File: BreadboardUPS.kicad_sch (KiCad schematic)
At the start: 3 parts, among them J2 Conn_01x04_Pin, J3 Conn_01x02_Pin, J4 Conn_01x02_Pin

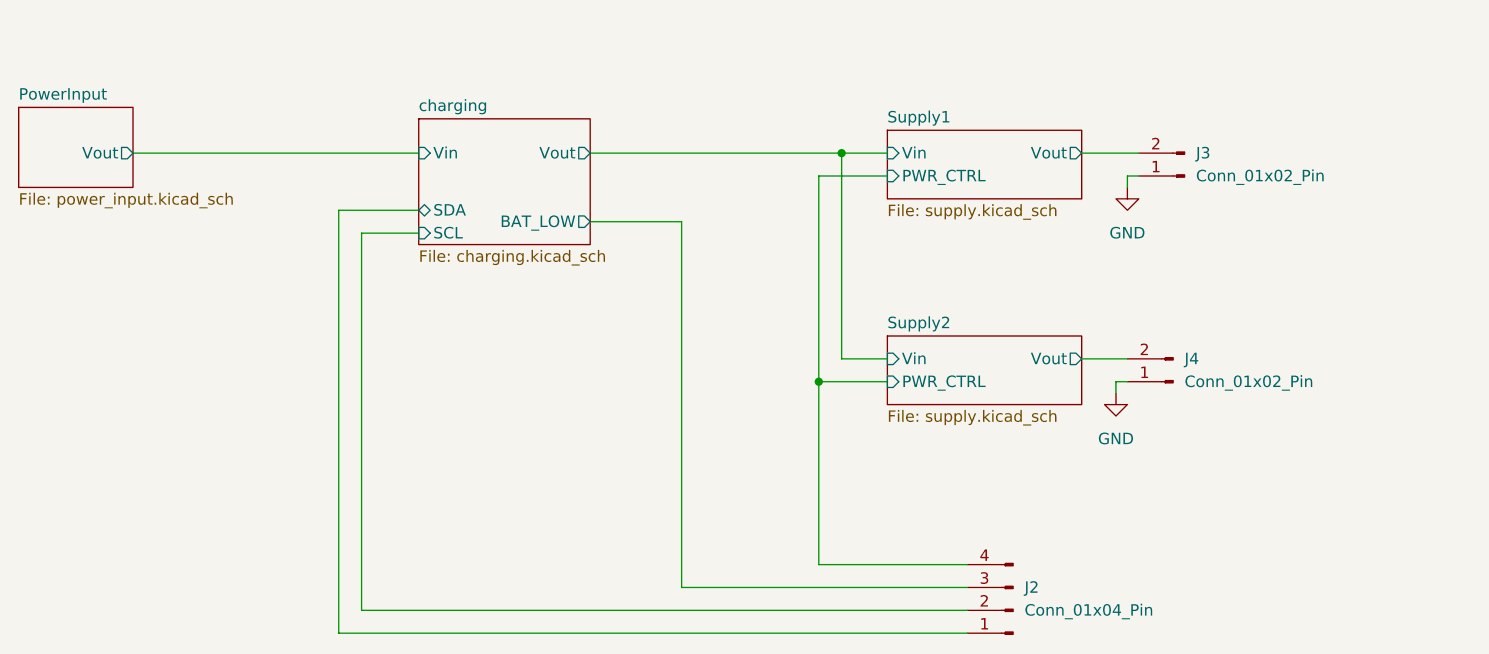
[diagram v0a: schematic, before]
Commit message: Solder jumpers for smaller simpler supply
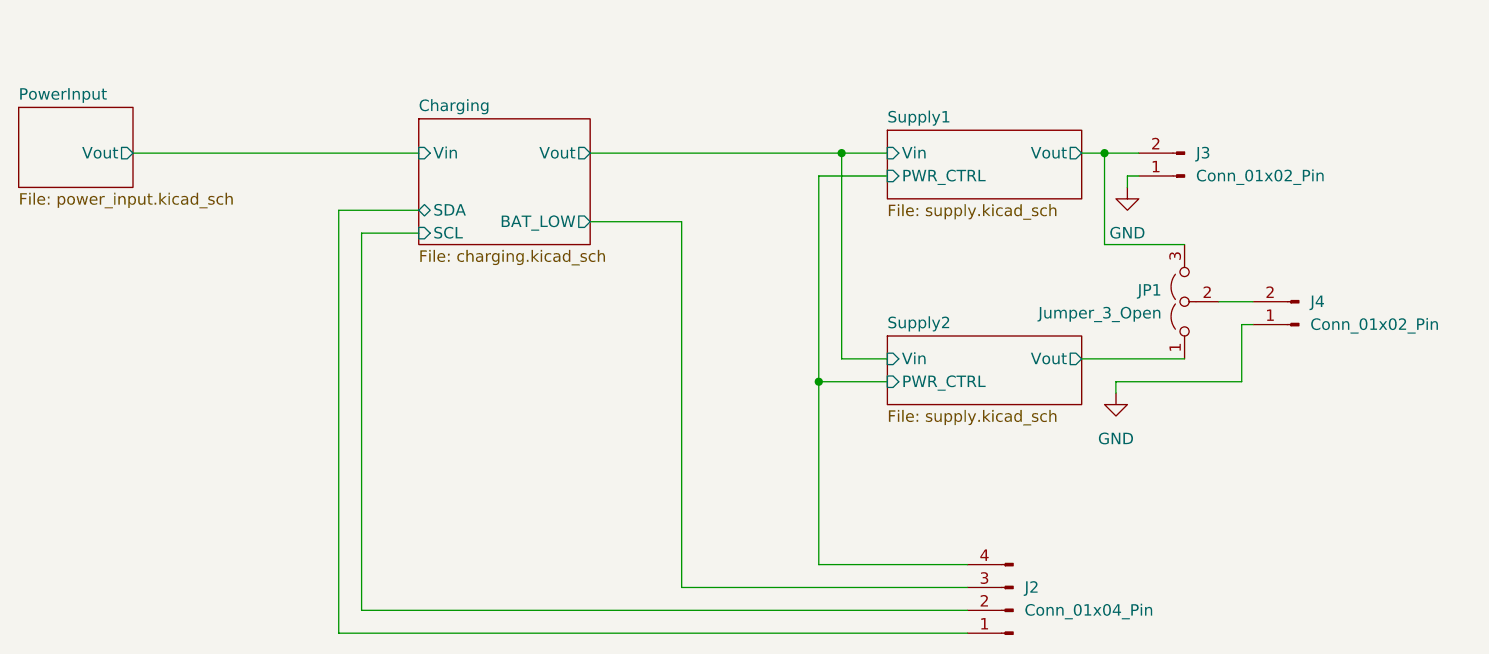
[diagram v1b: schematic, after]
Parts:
- added JP1: Jumper_3_Open, symbol Jumper:Jumper_3_Open
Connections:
- net Supply1/Vout: now also JP1.3 (B)
- net Supply2/Vout: now also JP1.1 (A); no longer J4.2 (Pin_2)
- new net: J4.2 (Pin_2), JP1.2 (C)
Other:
- sheet charging renamed Charging
- moved on the sheet: J4
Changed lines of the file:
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@@
+	)
+	(junction
+		(at 203.2 76.2)
+		(diameter 0)
+		(color 0 0 0 0)
 	)
 	(junction
@@
 	(wire
 		(pts
+			(xy 218.44 101.6) (xy 218.44 95.25)
+		)
+		(stroke
+			(width 0)
+			(type default)
+		)
+	)
+	(wire
+		(pts
 			(xy 171.45 101.6) (xy 171.45 121.92)
 		)
@@
 	(wire
 		(pts
-			(xy 204.47 101.6) (xy 205.74 101.6)
+			(xy 215.9 92.71) (xy 219.71 92.71)
 		)
 		(stroke
@@
 	(wire
 		(pts
+			(xy 200.66 99.06) (xy 212.09 99.06)
+		)
+		(stroke
+			(width 0)
+			(type default)
+		)
+	)
+	(wire
+		(pts
 			(xy 118.11 129.54) (xy 187.96 129.54)
 		)
@@
 	(wire
 		(pts
+			(xy 218.44 95.25) (xy 219.71 95.25)
+		)
+		(stroke
+			(width 0)
+			(type default)
+		)
+	)
+	(wire
+		(pts
+			(xy 203.2 76.2) (xy 207.01 76.2)
+		)
+		(stroke
+			(width 0)
+			(type default)
+		)
+	)
+	(wire
+		(pts
+			(xy 204.47 101.6) (xy 218.44 101.6)
+		)
+		(stroke
+			(width 0)
+			(type default)
+		)
+	)
+	(wire
+		(pts
 			(xy 120.65 127) (xy 187.96 127)
 		)
@@
 	(wire
 		(pts
+			(xy 203.2 86.36) (xy 203.2 76.2)
+		)
+		(stroke
+			(width 0)
+			(type default)
+		)
+	)
+	(wire
+		(pts
+			(xy 212.09 86.36) (xy 203.2 86.36)
+		)
+		(stroke
+			(width 0)
+			(type default)
+		)
+	)
+	(wire
+		(pts
 			(xy 171.45 121.92) (xy 187.96 121.92)
 		)
@@
 	(wire
 		(pts
-			(xy 200.66 76.2) (xy 207.01 76.2)
+			(xy 200.66 76.2) (xy 203.2 76.2)
 		)
 		(stroke
@@
 		(pts
 			(xy 205.74 78.74) (xy 205.74 80.01)
-		)
-		(stroke
-			(width 0)
-			(type default)
-		)
-	)
-	(wire
-		(pts
-			(xy 200.66 99.06) (xy 205.74 99.06)
 		)
 		(stroke
@@
 	(symbol
 		(lib_id "Connector:Conn_01x02_Pin")
-		(at 210.82 101.6 180)
+		(at 224.79 95.25 180)
 		(unit 1)
 		(exclude_from_sim no)
@@
 		(fields_autoplaced yes)
 		(property "Reference" "J4"
-			(at 212.09 99.0599 0)
+			(at 226.06 92.7099 0)
 			(effects
 				(font
@@
 		)
 		(property "Value" "Conn_01x02_Pin"
-			(at 212.09 101.5999 0)
+			(at 226.06 95.2499 0)
 			(effects
 				(font
@@
 		)
 		(property "Footprint" ""
-			(at 210.82 101.6 0)
+			(at 224.79 95.25 0)
 			(effects
 				(font
@@
 		)
 		(property "Datasheet" "~"
-			(at 210.82 101.6 0)
+			(at 224.79 95.25 0)
 			(effects
 				(font
@@
 		)
 		(property "Description" "Generic connector, single row, 01x02, script generated"
-			(at 210.82 101.6 0)
+			(at 224.79 95.25 0)
 			(effects
 				(font
@@
 		)
 	)
+	(symbol
+		(lib_id "Jumper:Jumper_3_Open")
+		(at 212.09 92.71 90)
+		(unit 1)
+		(exclude_from_sim no)
+		(in_bom no)
+		(on_board yes)
+		(dnp no)
+		(fields_autoplaced yes)
+		(property "Reference" "JP1"
+			(at 209.55 91.4399 90)
+			(effects
+				(font
+					(size 1.27 1.27)
+				)
+				(justify left)
+			)
+		)
+		(property "Value" "Jumper_3_Open"
+			(at 209.55 93.9799 90)
+			(effects
+				(font
+					(size 1.27 1.27)
+				)
+				(justify left)
+			)
+		)
+		(property "Footprint" ""
+			(at 212.09 92.71 0)
+			(effects
+				(font
+					(size 1.27 1.27)
+				)
+				(hide yes)
+			)
+		)
+		(property "Datasheet" "~"
+			(at 212.09 92.71 0)
+			(effects
+				(font
+					(size 1.27 1.27)
+				)
+				(hide yes)
+			)
+		)
+		(property "Description" "Jumper, 3-pole, both open"
+			(at 212.09 92.71 0)
+			(effects
+				(font
+					(size 1.27 1.27)
+				)
+				(hide yes)
+			)
+		)
+		(pin "3"
+		)
+		(pin "2"
+		)
+		(pin "1"
+		)
+		(instances
+			(project ""
+				(path "/3f1ccd97-6ac6-4e7a-a00a-840cd07719d8"
+					(reference "JP1")
+					(unit 1)
+				)
+			)
+		)
+	)
 	(sheet
 		(at 179.07 73.66)
@@
 			(color 0 0 0 0.0000)
 		)
-		(property "Sheetname" "charging"
+		(property "Sheetname" "Charging"
 			(at 127 71.6784 0)
 			(effects

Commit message: Part selection
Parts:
- removed JP1: Jumper_3_Open, symbol Jumper:Jumper_3_Open
- added JP101: SolderJumper_3_Open, Jumper:SolderJumper-3_P1.3mm_Open_RoundedPad1.0x1.5mm, symbol Jumper:SolderJumper_3_Open
- J101: renamed from J2; footprint (none) -> Connector_PinHeader_2.54mm:PinHeader_1x04_P2.54mm_Vertical; now left out of the parts list
- J102: renamed from J3; footprint (none) -> Connector_PinHeader_2.54mm:PinHeader_1x02_P2.54mm_Vertical; now left out of the parts list
- J103: renamed from J4; footprint (none) -> Connector_PinHeader_2.54mm:PinHeader_1x02_P2.54mm_Vertical; now left out of the parts list
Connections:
- net Supply1/Vout: now also JP101.3 (B)
- net Supply2/Vout: now also JP101.1 (A)
- net at J103.2 (Pin_2): now also JP101.2 (C)
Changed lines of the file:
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@@
+	(wire
+		(pts
+			(xy 212.09 86.36) (xy 212.09 87.63)
+		)
+		(stroke
+			(width 0)
+			(type default)
+		)
+	)
 	(wire
 		(pts
@@
 		(pts
 			(xy 173.99 76.2) (xy 179.07 76.2)
+		)
+		(stroke
+			(width 0)
+			(type default)
+		)
+	)
+	(wire
+		(pts
+			(xy 212.09 97.79) (xy 212.09 99.06)
 		)
 		(stroke
@@
 		(unit 1)
 		(exclude_from_sim no)
-		(in_bom yes)
+		(in_bom no)
 		(on_board yes)
 		(dnp no)
 		(fields_autoplaced yes)
-		(property "Reference" "J4"
+		(property "Reference" "J103"
 			(at 226.06 92.7099 0)
 			(effects
@@
 			)
 		)
-		(property "Footprint" ""
+		(property "Footprint" "Connector_PinHeader_2.54mm:PinHeader_1x02_P2.54mm_Vertical"
 			(at 224.79 95.25 0)
 			(effects
@@
 			(project "BreadboardUPS"
 				(path "/3f1ccd97-6ac6-4e7a-a00a-840cd07719d8"
-					(reference "J4")
+					(reference "J103")
 					(unit 1)
 				)
@@
 		(unit 1)
 		(exclude_from_sim no)
-		(in_bom yes)
+		(in_bom no)
 		(on_board yes)
 		(dnp no)
 		(fields_autoplaced yes)
-		(property "Reference" "J2"
+		(property "Reference" "J101"
 			(at 194.31 124.4599 0)
 			(effects
@@
 			)
 		)
-		(property "Footprint" ""
+		(property "Footprint" "Connector_PinHeader_2.54mm:PinHeader_1x04_P2.54mm_Vertical"
 			(at 193.04 127 0)
 			(effects
@@
 			(project ""
 				(path "/3f1ccd97-6ac6-4e7a-a00a-840cd07719d8"
-					(reference "J2")
+					(reference "J101")
 					(unit 1)
 				)
@@
 		(dnp no)
 		(fields_autoplaced yes)
-		(property "Reference" "#PWR015"
+		(property "Reference" "#PWR0101"
 			(at 204.47 109.22 0)
 			(effects
@@
 			(project "BreadboardUPS"
 				(path "/3f1ccd97-6ac6-4e7a-a00a-840cd07719d8"
-					(reference "#PWR015")
+					(reference "#PWR0101")
 					(unit 1)
 				)
@@
 		(unit 1)
 		(exclude_from_sim no)
-		(in_bom yes)
+		(in_bom no)
 		(on_board yes)
 		(dnp no)
 		(fields_autoplaced yes)
-		(property "Reference" "J3"
+		(property "Reference" "J102"
 			(at 213.36 76.1999 0)
 			(effects
@@
 			)
 		)
-		(property "Footprint" ""
+		(property "Footprint" "Connector_PinHeader_2.54mm:PinHeader_1x02_P2.54mm_Vertical"
 			(at 212.09 78.74 0)
 			(effects
@@
 			(project ""
 				(path "/3f1ccd97-6ac6-4e7a-a00a-840cd07719d8"
-					(reference "J3")
+					(reference "J102")
+					(unit 1)
+				)
+			)
+		)
+	)
+	(symbol
+		(lib_id "Jumper:SolderJumper_3_Open")
+		(at 212.09 92.71 90)
+		(unit 1)
+		(exclude_from_sim no)
+		(in_bom no)
+		(on_board yes)
+		(dnp no)
+		(fields_autoplaced yes)
+		(property "Reference" "JP101"
+			(at 209.55 91.4399 90)
+			(effects
+				(font
+					(size 1.27 1.27)
+				)
+				(justify left)
+			)
+		)
+		(property "Value" "SolderJumper_3_Open"
+			(at 209.55 93.9799 90)
+			(effects
+				(font
+					(size 1.27 1.27)
+				)
+				(justify left)
+			)
+		)
+		(property "Footprint" "Jumper:SolderJumper-3_P1.3mm_Open_RoundedPad1.0x1.5mm"
+			(at 212.09 92.71 0)
+			(effects
+				(font
+					(size 1.27 1.27)
+				)
+				(hide yes)
+			)
+		)
+		(property "Datasheet" "~"
+			(at 212.09 92.71 0)
+			(effects
+				(font
+					(size 1.27 1.27)
+				)
+				(hide yes)
+			)
+		)
+		(property "Description" "Solder Jumper, 3-pole, open"
+			(at 212.09 92.71 0)
+			(effects
+				(font
+					(size 1.27 1.27)
+				)
+				(hide yes)
+			)
+		)
+		(pin "2"
+		)
+		(pin "3"
+		)
+		(pin "1"
+		)
+		(instances
+			(project ""
+				(path "/3f1ccd97-6ac6-4e7a-a00a-840cd07719d8"
+					(reference "JP101")
 					(unit 1)
 				)
@@
 		(dnp no)
 		(fields_autoplaced yes)
-		(property "Reference" "#PWR014"
+		(property "Reference" "#PWR0102"
 			(at 205.74 86.36 0)
 			(effects
@@
 			(project "BreadboardUPS"
 				(path "/3f1ccd97-6ac6-4e7a-a00a-840cd07719d8"
-					(reference "#PWR014")
+					(reference "#PWR0102")
 					(unit 1)
 				)
-			)
-		)
-	)
-	(symbol
-		(lib_id "Jumper:Jumper_3_Open")
-		(at 212.09 92.71 90)
-		(unit 1)
-		(exclude_from_sim no)
-		(in_bom no)
-		(on_board yes)
-		(dnp no)
-		(fields_autoplaced yes)
-		(property "Reference" "JP1"
-			(at 209.55 91.4399 90)
-			(effects
-				(font
-					(size 1.27 1.27)
-				)
-				(justify left)
-			)
-		)
-		(property "Value" "Jumper_3_Open"
-			(at 209.55 93.9799 90)
-			(effects
-				(font
-					(size 1.27 1.27)
-				)
-				(justify left)
-			)
-		)
-		(property "Footprint" ""
-			(at 212.09 92.71 0)
-			(effects
-				(font
-					(size 1.27 1.27)
-				)
-				(hide yes)
-			)
-		)
-		(property "Datasheet" "~"
-			(at 212.09 92.71 0)
-			(effects
-				(font
-					(size 1.27 1.27)
-				)
-				(hide yes)
-			)
-		)
-		(property "Description" "Jumper, 3-pole, both open"
-			(at 212.09 92.71 0)
-			(effects
-				(font
-					(size 1.27 1.27)
-				)
-				(hide yes)
-			)
-		)
-		(pin "3"
-		)
-		(pin "2"
-		)
-		(pin "1"
-		)
-		(instances
-			(project ""
-				(path "/3f1ccd97-6ac6-4e7a-a00a-840cd07719d8"
-					(reference "JP1")
-					(unit 1)
-				)

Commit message: Connection naming
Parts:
- removed J101: Conn_01x04_Pin, Connector_PinHeader_2.54mm:PinHeader_1x04_P2.54mm_Vertical, symbol Connector:Conn_01x04_Pin
- added J101: Output1, Connector_PinHeader_2.54mm:PinHeader_1x02_P2.54mm_Vertical, symbol Connector:Conn_01x02_Pin
- added J104: Ctrl, Connector_PinHeader_2.54mm:PinHeader_1x05_P2.54mm_Vertical, symbol Connector:Conn_01x05_Pin
- added J105, J106, J107: Output2, Connector_PinHeader_2.54mm:PinHeader_1x02_P2.54mm_Vertical, symbol Connector:Conn_01x02_Pin
- J102, J103: value Conn_01x02_Pin -> Output1
- JP101: value SolderJumper_3_Open -> Single/Dual Supply
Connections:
- net GND: now also J102.2 (Pin_2), J103.2 (Pin_2), J101.2 (Pin_2), J105.2 (Pin_2), J106.2 (Pin_2), J107.2 (Pin_2); no longer J102.1 (Pin_1), J103.1 (Pin_1)
- net Supply1/Vout: now also J102.1 (Pin_1), J103.1 (Pin_1), J101.1 (Pin_1); no longer J102.2 (Pin_2)
- net at JP101.2 (C): now also J105.1 (Pin_1), J106.1 (Pin_1), J107.1 (Pin_1); no longer J103.2 (Pin_2)
- new net BAT_LOW: J104.3 (Pin_3)
- new net PFM: J104.1 (Pin_1)
- new net PWR_CTRL: J104.2 (Pin_2)
- new net SCL: J104.5 (Pin_5)
- new net SDA: J104.4 (Pin_4)
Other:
- sheet Supply1 ports: added PFM; removed none
- sheet Supply2 ports: added PFM; removed none

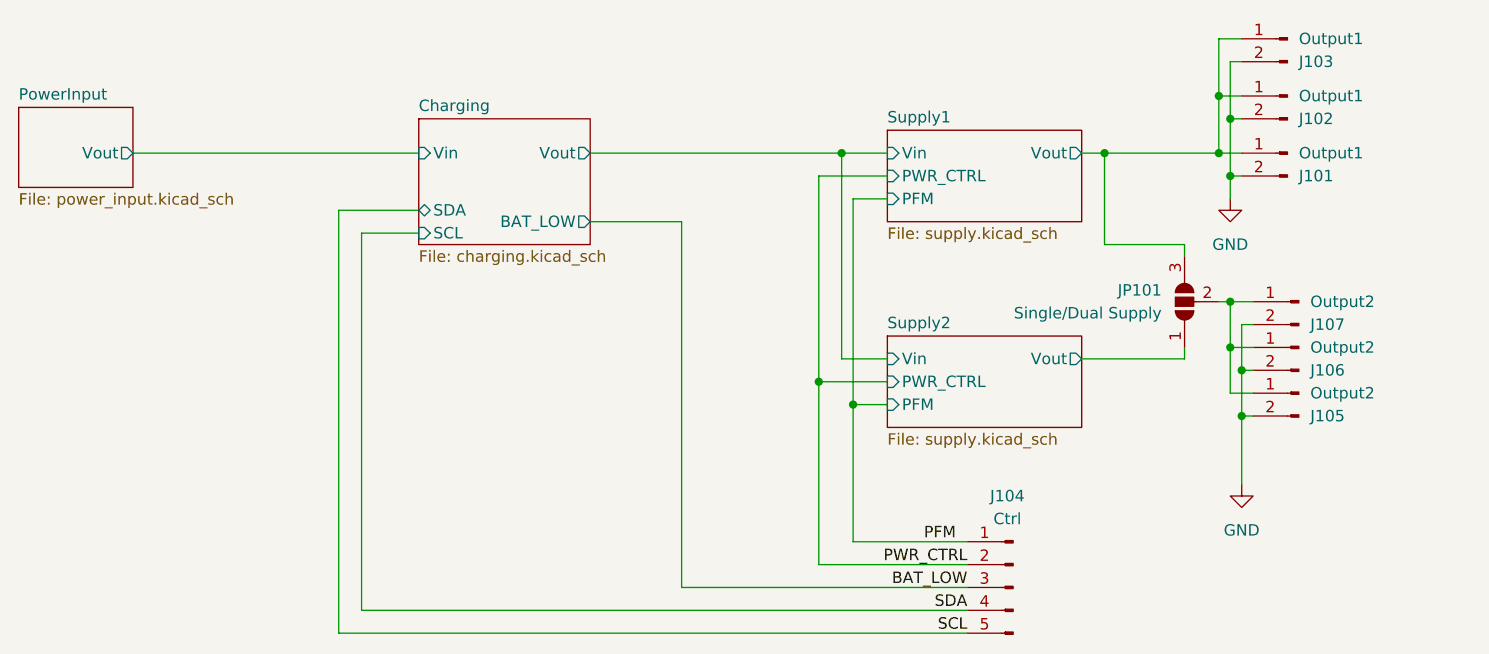
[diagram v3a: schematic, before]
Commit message: Remove dual supply
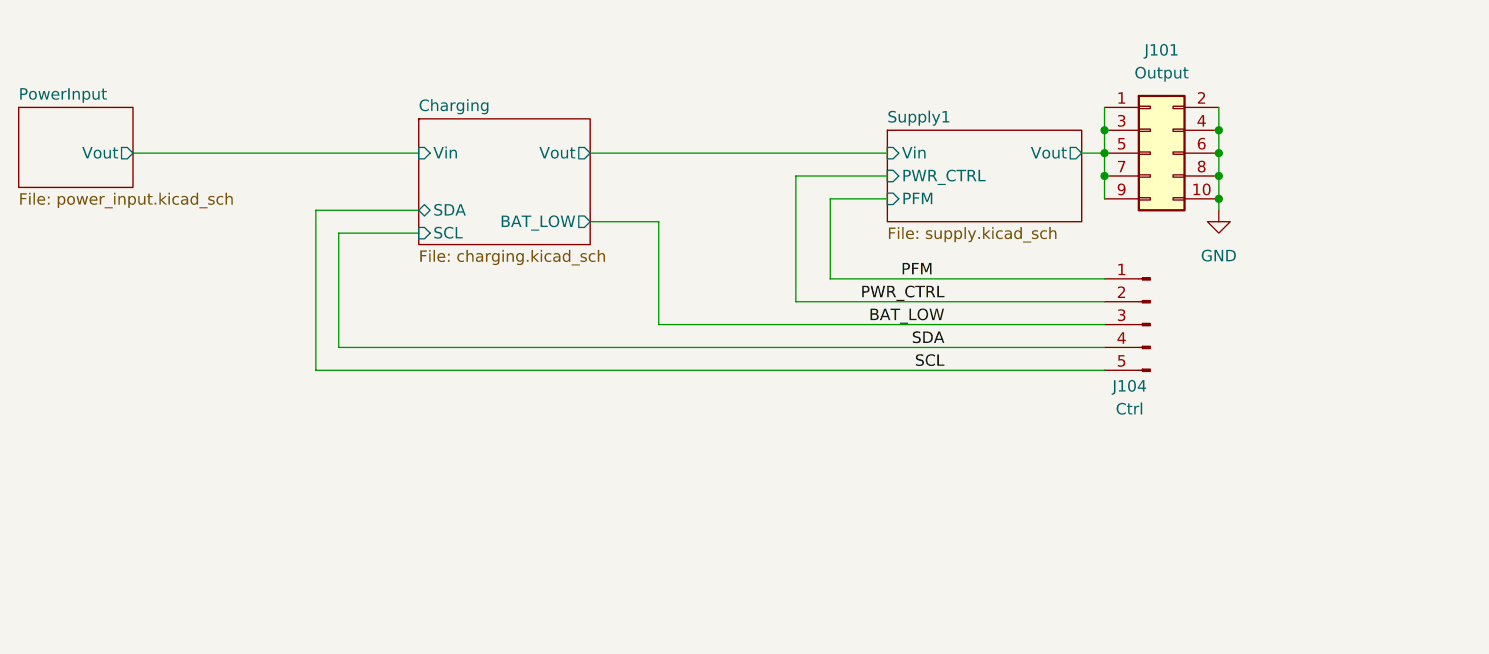
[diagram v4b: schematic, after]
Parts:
- removed J101, J102, J103: Output1, Connector_PinHeader_2.54mm:PinHeader_1x02_P2.54mm_Vertical, symbol Connector:Conn_01x02_Pin
- removed J105, J106, J107: Output2, Connector_PinHeader_2.54mm:PinHeader_1x02_P2.54mm_Vertical, symbol Connector:Conn_01x02_Pin
- removed JP101: Single/Dual Supply, Jumper:SolderJumper-3_P1.3mm_Open_RoundedPad1.0x1.5mm, symbol Jumper:SolderJumper_3_Open
- added J101: Output, Connector_PinHeader_2.54mm:PinHeader_2x05_P2.54mm_Vertical, symbol Connector_Generic:Conn_02x05_Odd_Even
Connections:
- net GND: now also J101.10 (Pin_10), J101.2 (Pin_2), J101.4 (Pin_4), J101.6 (Pin_6), J101.8 (Pin_8)
- net Supply1/Vout: now also J101.1 (Pin_1), J101.3 (Pin_3), J101.5 (Pin_5), J101.7 (Pin_7), J101.9 (Pin_9)
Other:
- removed sheet Supply2
- moved on the sheet: J104

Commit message: Update BOM options for export
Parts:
- J101, J104: now left out of the parts list
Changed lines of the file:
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@@
 		(unit 1)
 		(exclude_from_sim no)
-		(in_bom yes)
+		(in_bom no)
 		(on_board yes)
 		(dnp no)
@@
 		(unit 1)
 		(exclude_from_sim no)
-		(in_bom yes)
+		(in_bom no)
 		(on_board yes)
 		(dnp no)
